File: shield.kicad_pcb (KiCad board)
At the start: 4 copper layers, 150 x 120 mm, 146 parts, among them J1 NAPPE_ADC1, J10 OLED_SPI_2x8, J13 NAPPE_GPIO2, J14 NAPPE_COM, J2 NAPPE_ADC2, J3 NAPPE_PWM, J4 NAPPE_GPIO1, J5 DEVKIT_C2000_ROW_A, J6 DEVKIT_C2000_ROW_B, J7 ESP32_C6_DEVKITC_1_J1, J8 ESP32_C6_DEVKITC_1_J3, J9 J_PWR_11-25V, U1 LDO_3V3_ISO, U2 NCM3S1205MC, U3 NCM3S1205MC, U4 ER-OLEDM032-1

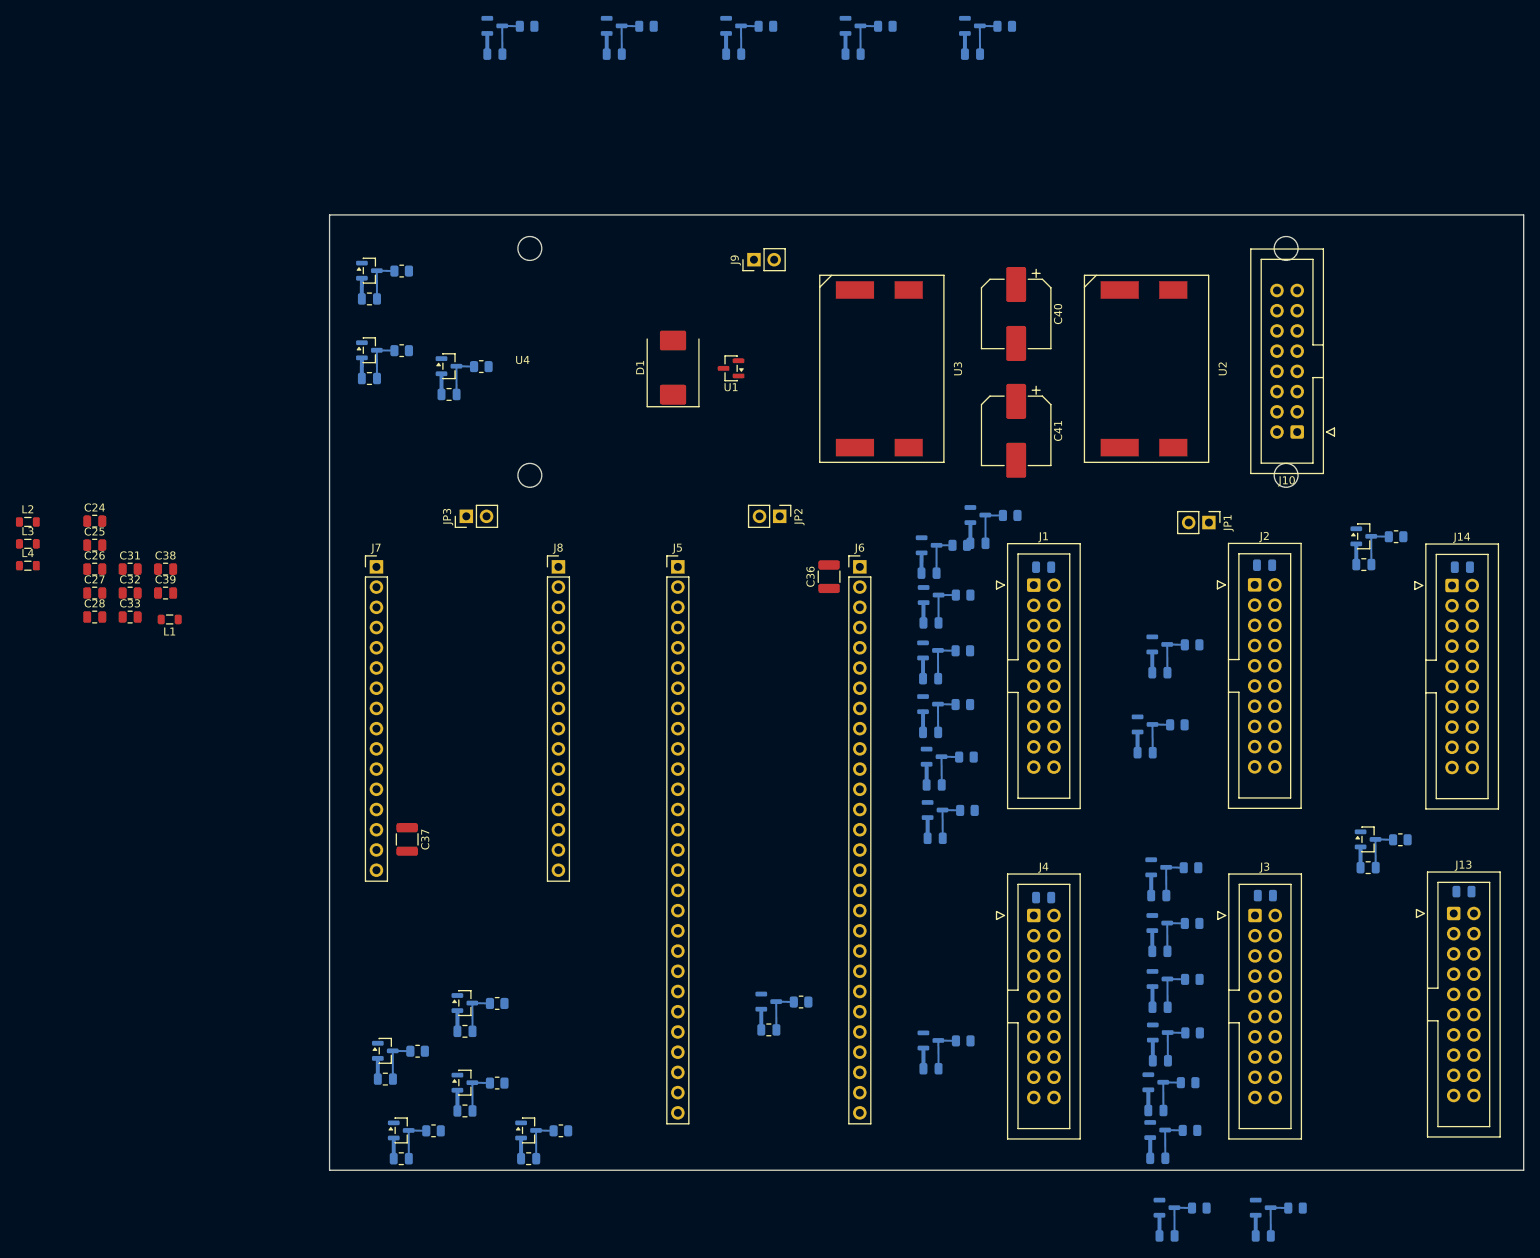
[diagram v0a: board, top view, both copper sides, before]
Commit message: Placement manuel des 11 trios de protection nappe sur le PCB
Repositionnement a la main (GUI KiCad) des composants places/groupes
par script en phase B, pour un agencement pratique pres de leurs
connecteurs respectifs.
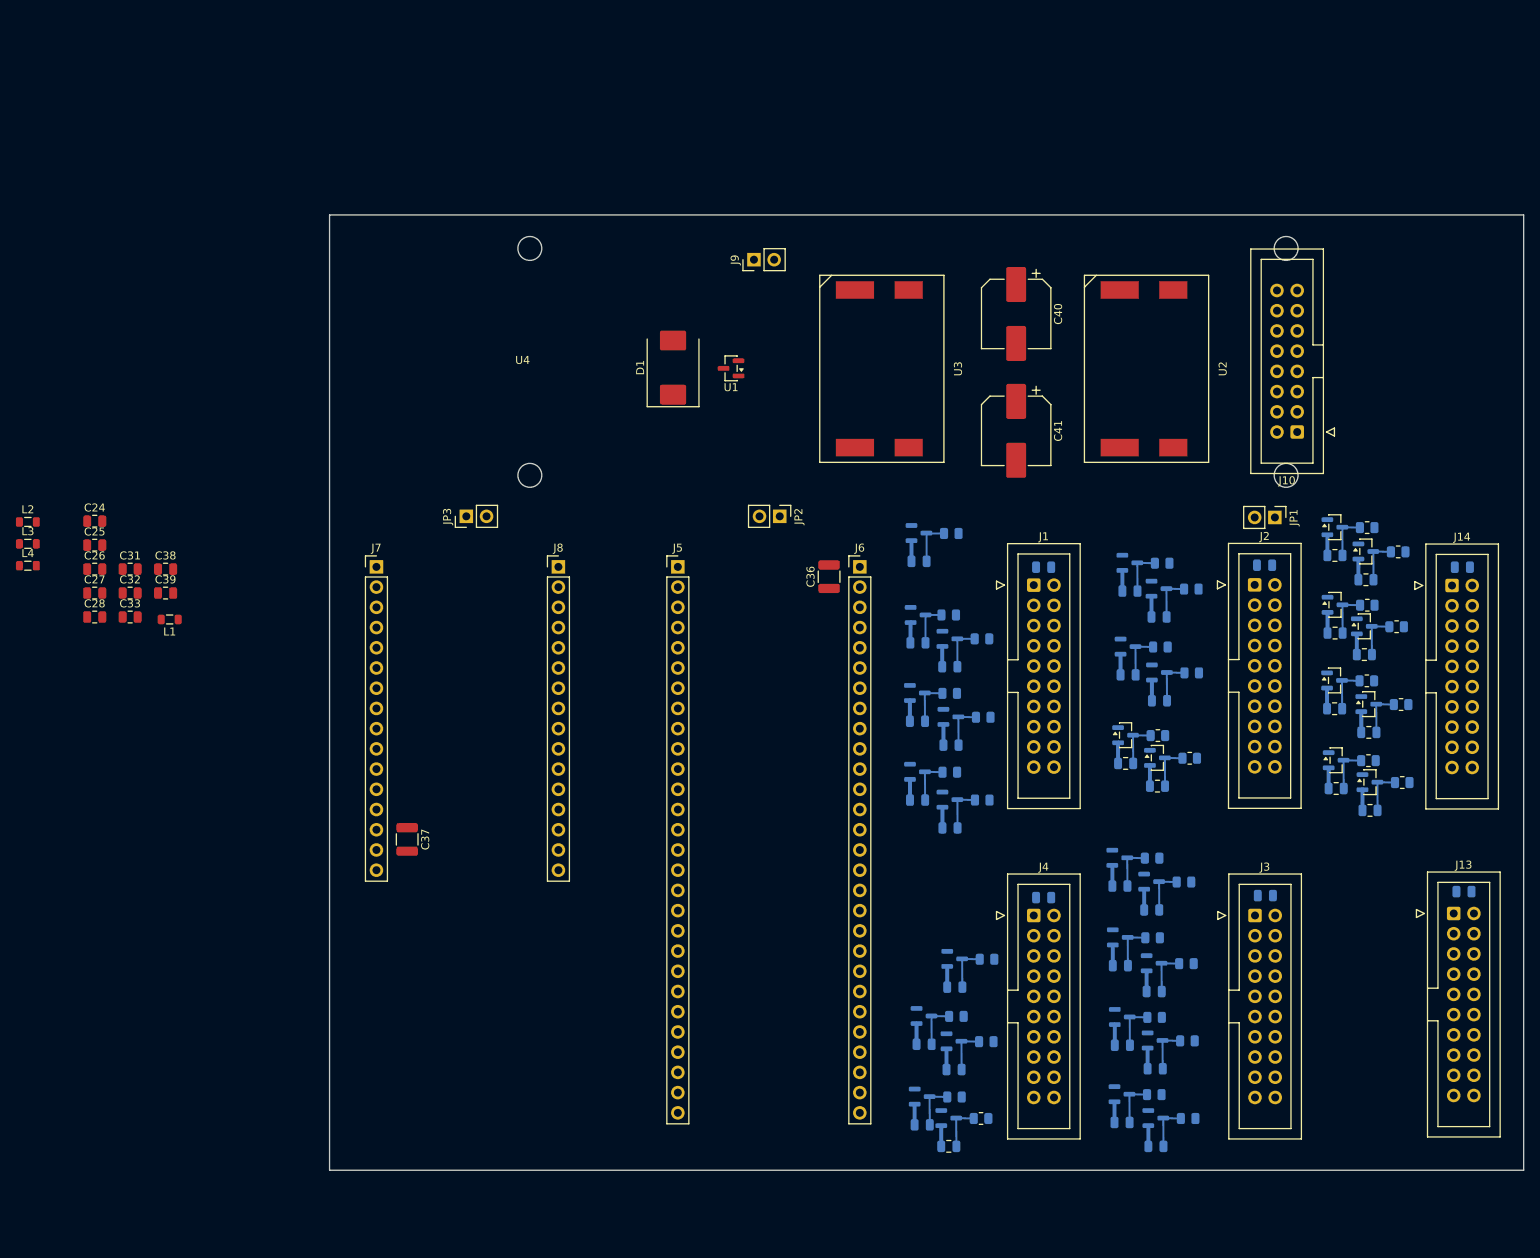
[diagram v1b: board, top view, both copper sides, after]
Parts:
- moved D28 139.6 mm to (235.5, 73.0)
- moved R27 139.6 mm to (239.6, 73.0)
- moved C47 139.6 mm to (235.5, 76.5)
- moved C23 136.6 mm to (183.7, 148.1)
- moved D24 136.6 mm to (183.7, 144.5)
- moved R23 136.6 mm to (187.8, 144.6)
- moved D22 134.5 mm to (187.7, 137.6)
- moved C21 134.5 mm to (187.7, 141.1)
- moved R21 134.5 mm to (191.8, 137.6)
- moved C50 134.0 mm to (239.2, 89.0)
- moved D31 134.0 mm to (239.2, 85.4)
- moved R30 134.0 mm to (243.3, 85.5)
- moved D32 131.7 mm to (235.5, 92.2)
- moved R31 131.7 mm to (239.5, 92.3)
- moved C51 131.7 mm to (235.5, 95.8)
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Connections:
- J2 pad 11: I_SHUNT2_CMP -> I_SHUNT1_CMP
- J2 pad 13: unconnected-(J2-RESERVE_ADC2_1-Pad13) -> I_SHUNT2_CMP
- J2 pad 3: I_shunt1 -> VREFLO_SENSE
- J2 pad 5: I_shunt2 -> VREF_ADC
- J2 pad 7: VREF_ADC -> I_shunt1
- J2 pad 8: VREFLO_SENSE -> GND
- J2 pad 9: I_SHUNT1_CMP -> I_shunt2
- J5 pad 22: I_SHUNT1_CMP -> I_SHUNT1_CMP_MCU
- J5 pad 26: I_SHUNT2_CMP -> I_SHUNT2_CMP_MCU

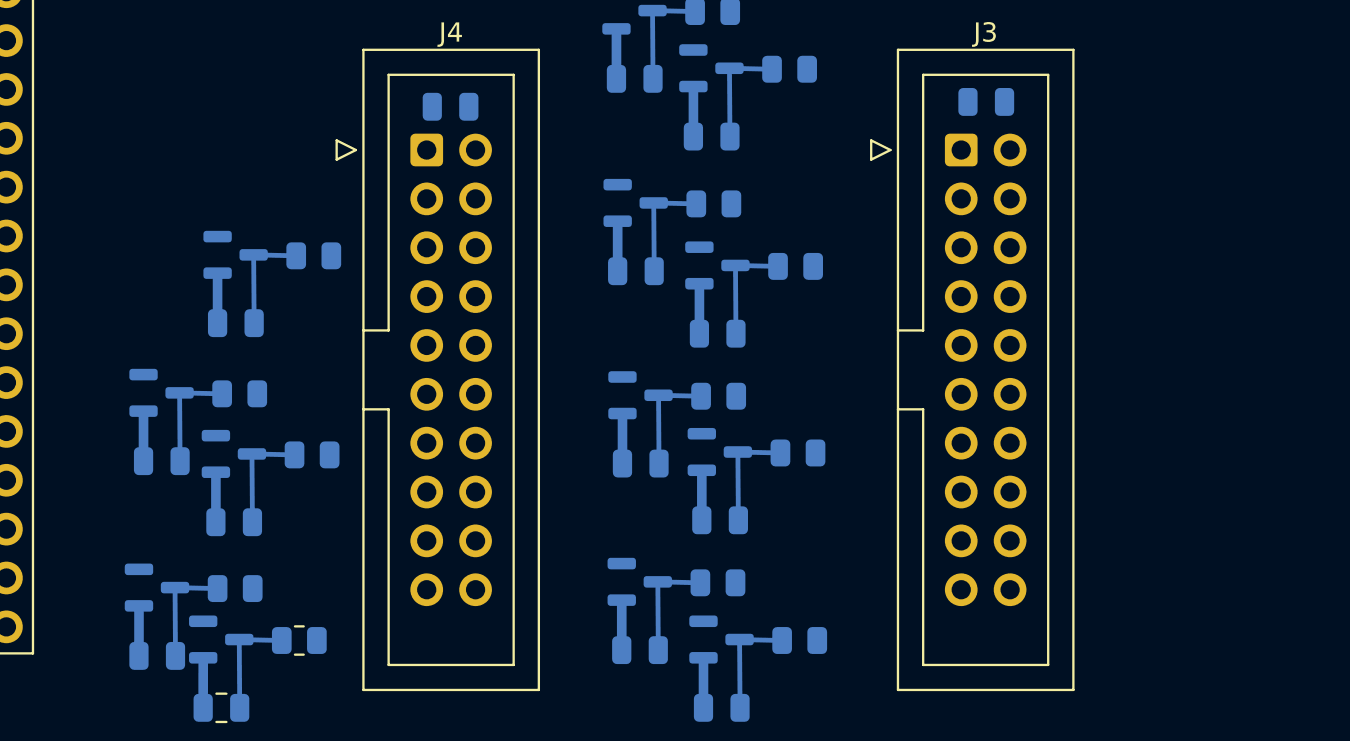
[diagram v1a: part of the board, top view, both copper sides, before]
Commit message: PCB : place, route et groupe les 4 trios Stage1_EN/Stage2_EN/HV_EN/Discharge
Update PCB from Schematic (12 nouveaux footprints), miroir F.Cu->B.Cu
un par un, places pres de J4 (nappe GPIO-1) et J13 (nappe logic),
routage interne (1 masse + 2 noeuds _MCU par trio, meme motif que les
34 trios existants), groupes PROT_<signal>_MCU.

DRC : unconnected_items -12 (4 trios x 3 connexions), aucune nouvelle
categorie de violation imputable aux nouveaux designateurs (D36-39/
R35-38/C55-58) - verifie par grep, uniquement les memes categories
cosmetiques deja presentes sur les 34 trios existants.
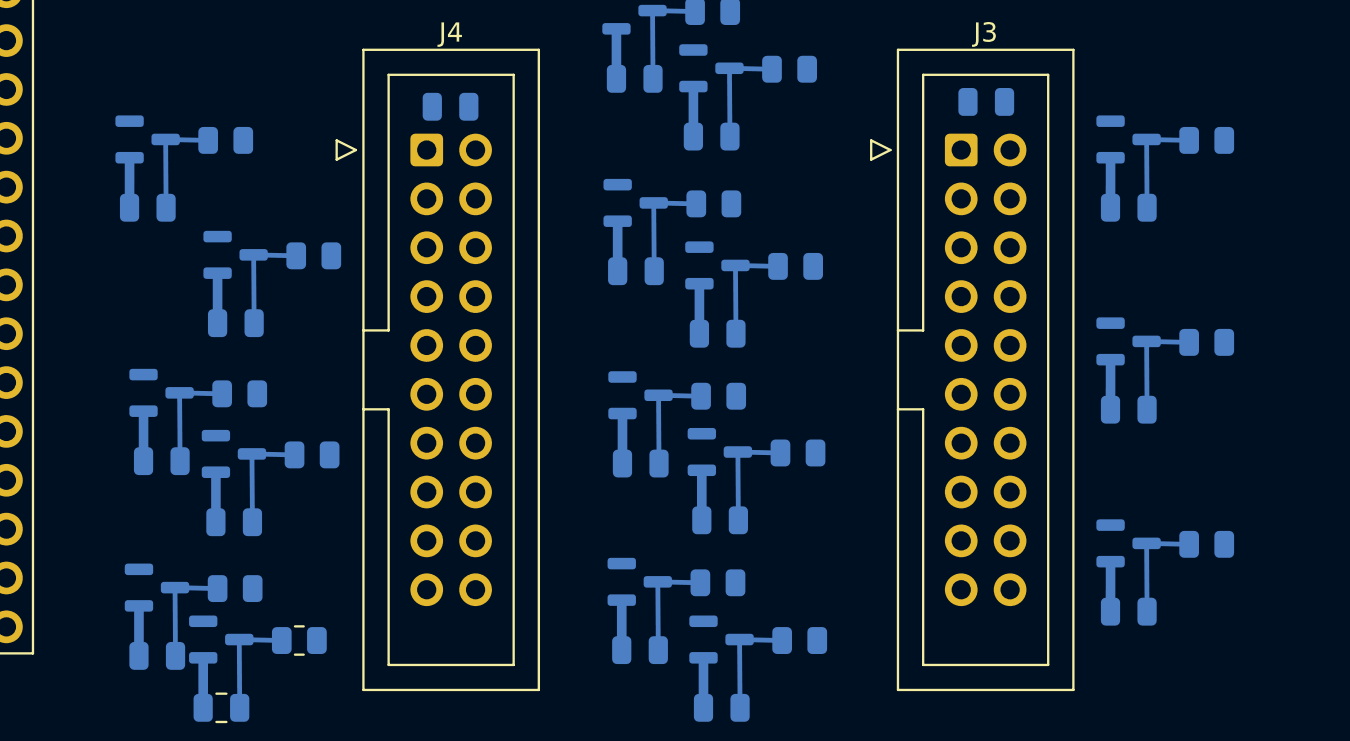
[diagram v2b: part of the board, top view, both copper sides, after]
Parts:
- added C55: 100pF, Capacitor_SMD:C_0805_2012Metric, B.Cu at (183.2, 124.8)
- added C56: 100pF, Capacitor_SMD:C_0805_2012Metric, B.Cu at (234.2, 124.8)
- added C57: 100pF, Capacitor_SMD:C_0805_2012Metric, B.Cu at (234.2, 135.2)
- added C58: 100pF, Capacitor_SMD:C_0805_2012Metric, B.Cu at (234.2, 145.8)
- added D36: BAT54S, Package_TO_SOT_SMD:SOT-23, B.Cu at (183.2, 121.2)
- added D37: BAT54S, Package_TO_SOT_SMD:SOT-23, B.Cu at (234.2, 121.2)
- added D38: BAT54S, Package_TO_SOT_SMD:SOT-23, B.Cu at (234.2, 131.7)
- added D39: BAT54S, Package_TO_SOT_SMD:SOT-23, B.Cu at (234.2, 142.2)
- added R35: 10R, Resistor_SMD:R_0805_2012Metric, B.Cu at (187.3, 121.2)
- added R36: 10R, Resistor_SMD:R_0805_2012Metric, B.Cu at (238.3, 121.2)
- added R37: 10R, Resistor_SMD:R_0805_2012Metric, B.Cu at (238.3, 131.8)
- added R38: 10R, Resistor_SMD:R_0805_2012Metric, B.Cu at (238.3, 142.2)
- J13: value NAPPE_GPIO2 -> NAPPE_LOGIC
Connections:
- net nFAULT_MCU renamed ~{FAULT_MCU}
- net nRESET renamed ~{RESET}
- J13 pad 11: unconnected-(J13-RESERVE_GPIO2_5-Pad11) -> CAN_RX
- J13 pad 13: unconnected-(J13-RESERVE_GPIO2_6-Pad13) -> CAN_TX
- J13 pad 15: unconnected-(J13-RESERVE_GPIO2_7-Pad15) -> PWM2_B
- J13 pad 17: unconnected-(J13-RESERVE_GPIO2_8-Pad17) -> PWM3_B
- J13 pad 19: unconnected-(J13-RESERVE_GPIO2_9-Pad19) -> PWM4_B
- J13 pad 3: unconnected-(J13-RESERVE_GPIO2_1-Pad3) -> Stage1_EN
- J13 pad 5: unconnected-(J13-RESERVE_GPIO2_2-Pad5) -> Stage2_EN
- J13 pad 7: unconnected-(J13-RESERVE_GPIO2_3-Pad7) -> HV_EN
- J13 pad 9: unconnected-(J13-RESERVE_GPIO2_4-Pad9) -> Discharge
- J5 pad 10: GND -> ADC_8
- J5 pad 11: Iout_MCU -> GND
- J5 pad 12: ADC_8 -> ADC_9
- J5 pad 13: GND -> ADC_10
- J5 pad 14: ADC_9 -> ADC_11
- J5 pad 15: ADC_10 -> ADC_12
- J5 pad 17: ADC_11 -> I_SHUNT1_CMP_MCU
- J5 pad 18: ADC_12 -> I_shunt1_MCU
- J5 pad 20: I_shunt1_MCU -> I_SHUNT2_CMP_MCU
- J5 pad 21: GND -> I_shunt2_MCU
- J5 pad 22: I_SHUNT1_CMP_MCU -> GND
- J5 pad 23: GND -> Stage1_EN_MCU
- J5 pad 24: I_shunt2_MCU -> Stage2_EN_MCU
- J5 pad 25: GND -> HV_EN_MCU
- J5 pad 26: I_SHUNT2_CMP_MCU -> Discharge_MCU
- J5 pad 4: GND -> Iin_MCU
- J5 pad 5: V1_MCU -> Iout_MCU
- J5 pad 6: Temp1_MCU -> GND
- J5 pad 7: GND -> V1_MCU
- J5 pad 8: Temp2_MCU -> Temp1_MCU
- J5 pad 9: Iin_MCU -> Temp2_MCU
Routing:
- net GND: track 88.3 -> 98.7 mm
- net HV_EN_MCU: track 0.00 -> 5.76 mm
- net Discharge_MCU: track 0.00 -> 5.76 mm
- net Stage2_EN_MCU: track 0.00 -> 5.76 mm
- net Stage1_EN_MCU: track 0.00 -> 5.76 mm
